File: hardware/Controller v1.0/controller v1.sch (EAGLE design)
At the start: 36 parts, among them CON1 1X08-CONN3.5MM, CON2 1X08-CONN3.5MM, CON3 1X08-CONN3.5MM, CON4 1X08-CONN3.5MM, IC1 MC33880PEG, IC2 L293DD, IC3 MC33880PEG

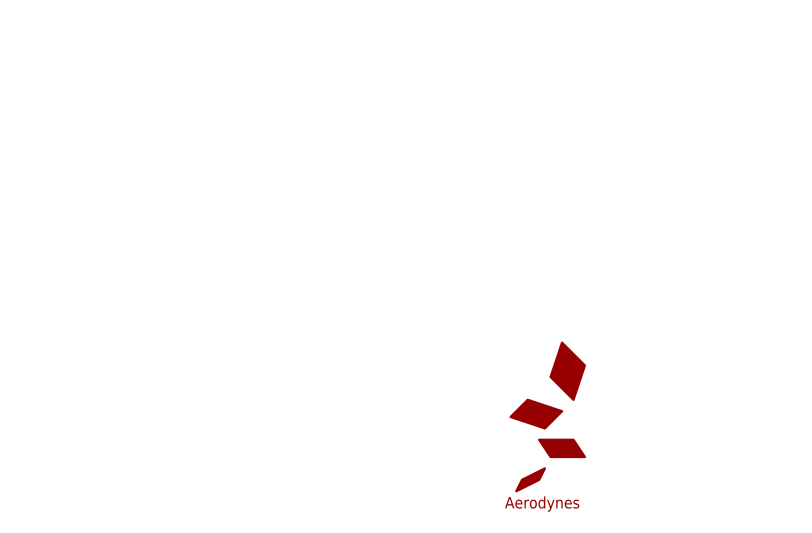
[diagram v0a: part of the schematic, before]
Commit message: Added license/author into on schematics
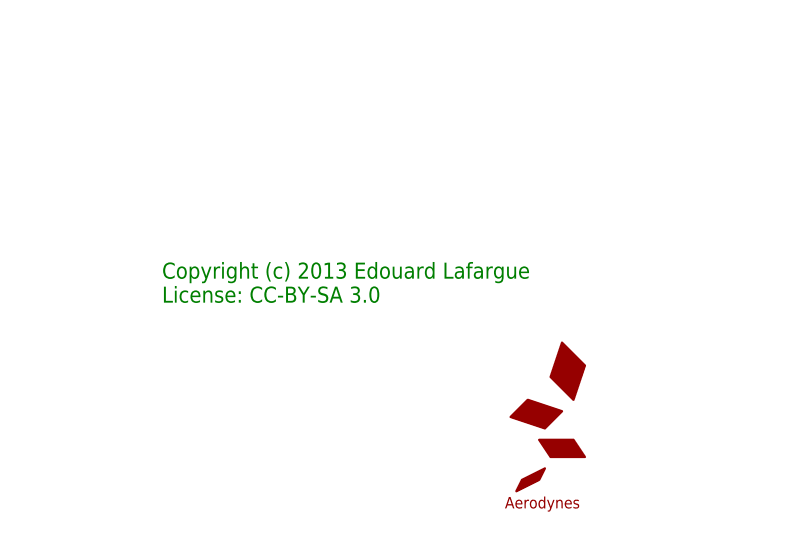
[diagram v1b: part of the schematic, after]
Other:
- note added: "Copyright (c) 2013 Edouard Lafargue License: CC-BY-SA 3.0"
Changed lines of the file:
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@@
 <text x="129.54" y="-40.64" size="1.778" layer="91">R6 at 10k leads to CURR_MEASURE
 at 5V for 1A input current.</text>
+<text x="256.54" y="-22.86" size="1.778" layer="91">Copyright (c) 2013 Edouard Lafargue
+License: CC-BY-SA 3.0</text>
 </plain>
 <instances>

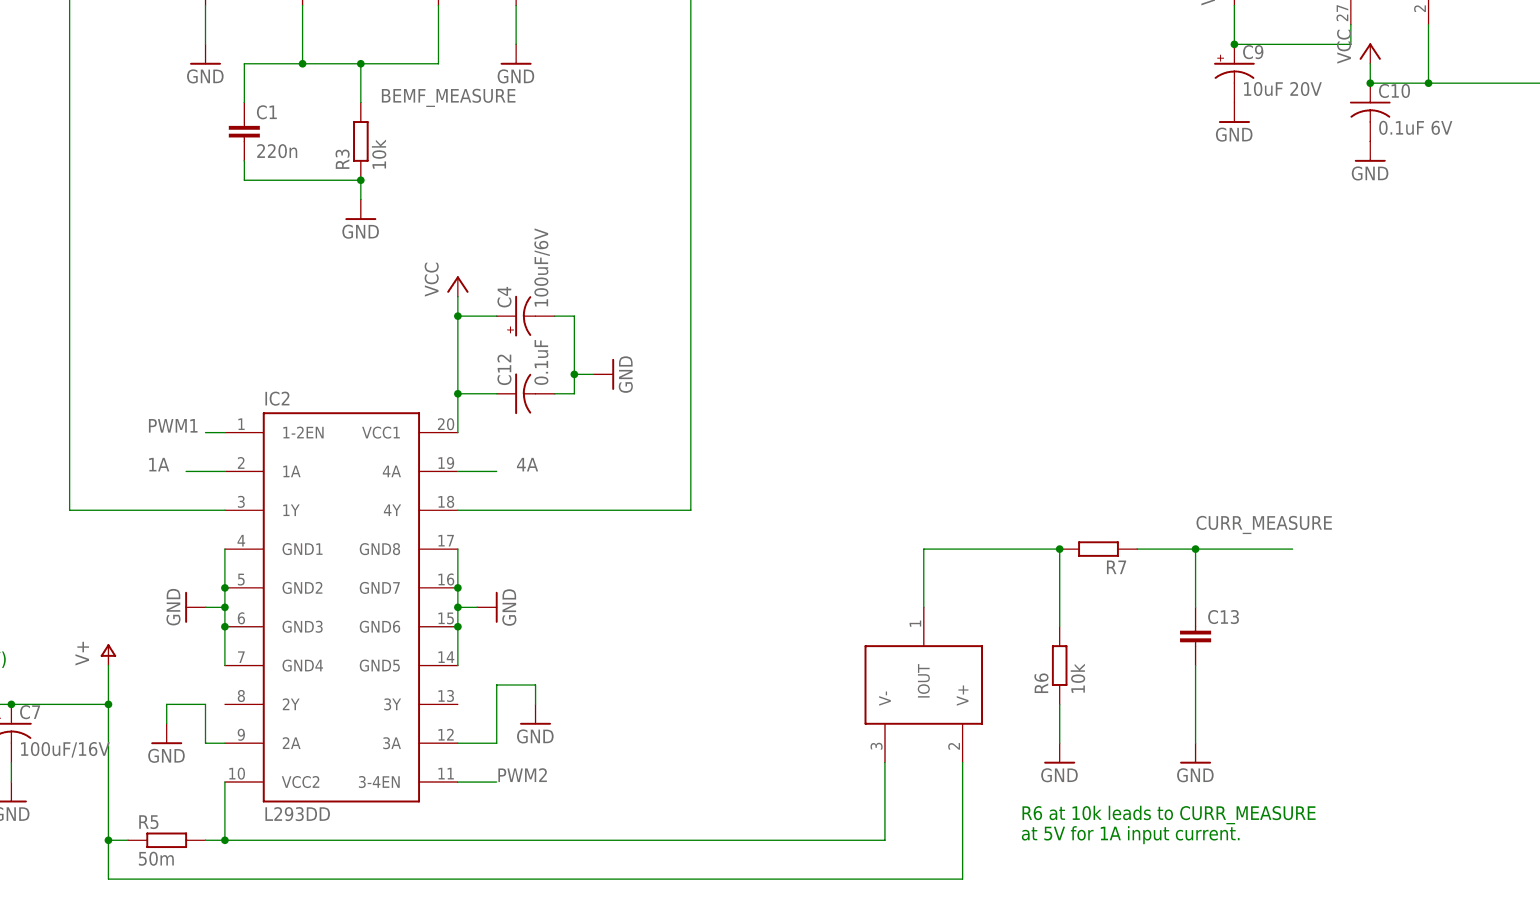
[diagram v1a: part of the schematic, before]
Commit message: Updates to match exactly first working prototype
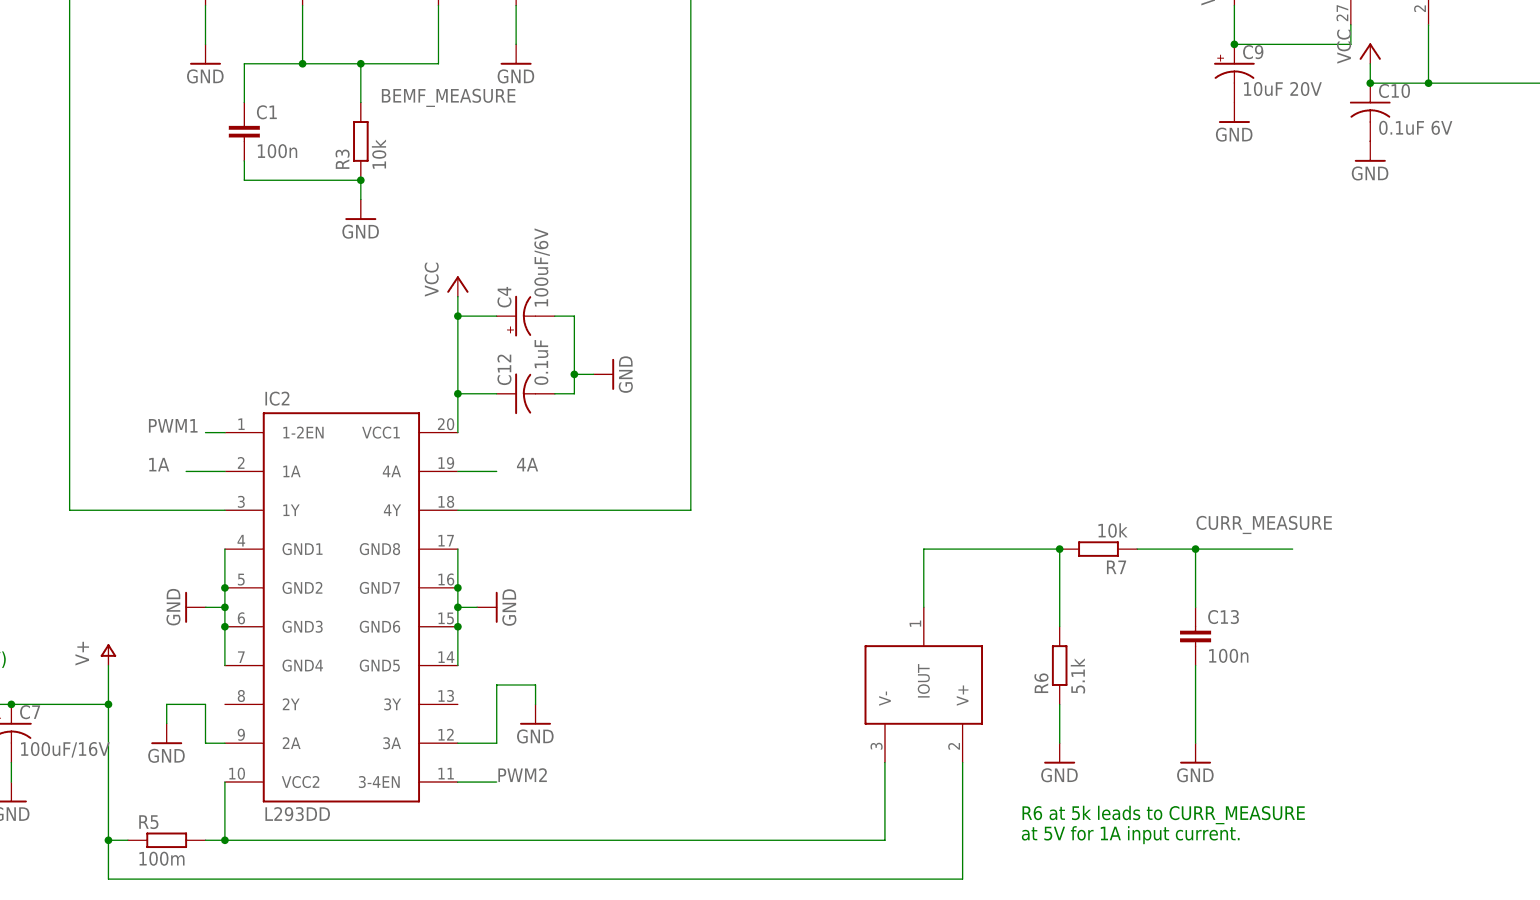
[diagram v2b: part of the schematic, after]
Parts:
- C1: value 220n -> 100n
- C13: value (none) -> 100n
- R5: value 50m -> 100m
- R6: value 10k -> 5.1k
- R7: value (none) -> 10k
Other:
- note added: "R6 at 5k leads to CURR_MEASURE at 5V for 1A input current."
- note removed: "R6 at 10k leads to CURR_MEASURE at 5V for 1A input current."
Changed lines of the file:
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@@
 <part name="SL2" library="adafruit" deviceset="1X2" device="-3.5MM"/>
 <part name="GND5" library="supply1" deviceset="GND" device=""/>
-<part name="C1" library="resistor" deviceset="C-EU" device="C0805" value="220n"/>
+<part name="C1" library="resistor" deviceset="C-EU" device="C0805" value="100n"/>
 <part name="C2" library="rcl-ez" deviceset="C-US" device="025-025X050" value="0.1uF"/>
 <part name="GND6" library="supply1" deviceset="GND" device=""/>
@@
 <part name="GND19" library="supply1" deviceset="GND" device=""/>
 <part name="GND20" library="supply1" deviceset="GND" device=""/>
-<part name="R5" library="resistor" deviceset="R-EU_" device="M1206" value="50m"/>
-<part name="R6" library="resistor" deviceset="R-EU_" device="R0603" value="10k"/>
-<part name="R7" library="resistor" deviceset="R-EU_" device="R0603"/>
+<part name="R5" library="resistor" deviceset="R-EU_" device="M1206" value="100m"/>
+<part name="R6" library="resistor" deviceset="R-EU_" device="R0603" value="5.1k"/>
+<part name="R7" library="resistor" deviceset="R-EU_" device="R0603" value="10k"/>
 <part name="GND21" library="supply1" deviceset="GND" device=""/>
 <part name="GND22" library="supply1" deviceset="GND" device=""/>
-<part name="C13" library="resistor" deviceset="C-EU" device="C0805K"/>
+<part name="C13" library="resistor" deviceset="C-EU" device="C0805K" value="100n"/>
 <part name="U$3" library="aerodynes" deviceset="ZXCT1009" device="-F"/>
 <part name="JP1" library="jumper" deviceset="JP1E" device=""/>
@@
 <text x="228.6" y="132.08" size="1.778" layer="91">Bank 4</text>
 <text x="144.78" y="203.2" size="1.778" layer="91">"wire to board Eurostyle terminal blocks"</text>
-<text x="129.54" y="-40.64" size="1.778" layer="91">R6 at 10k leads to CURR_MEASURE
+<text x="129.54" y="-40.64" size="1.778" layer="91">R6 at 5k leads to CURR_MEASURE
 at 5V for 1A input current.</text>
 <text x="256.54" y="-22.86" size="1.778" layer="91">Copyright (c) 2013 Edouard Lafargue

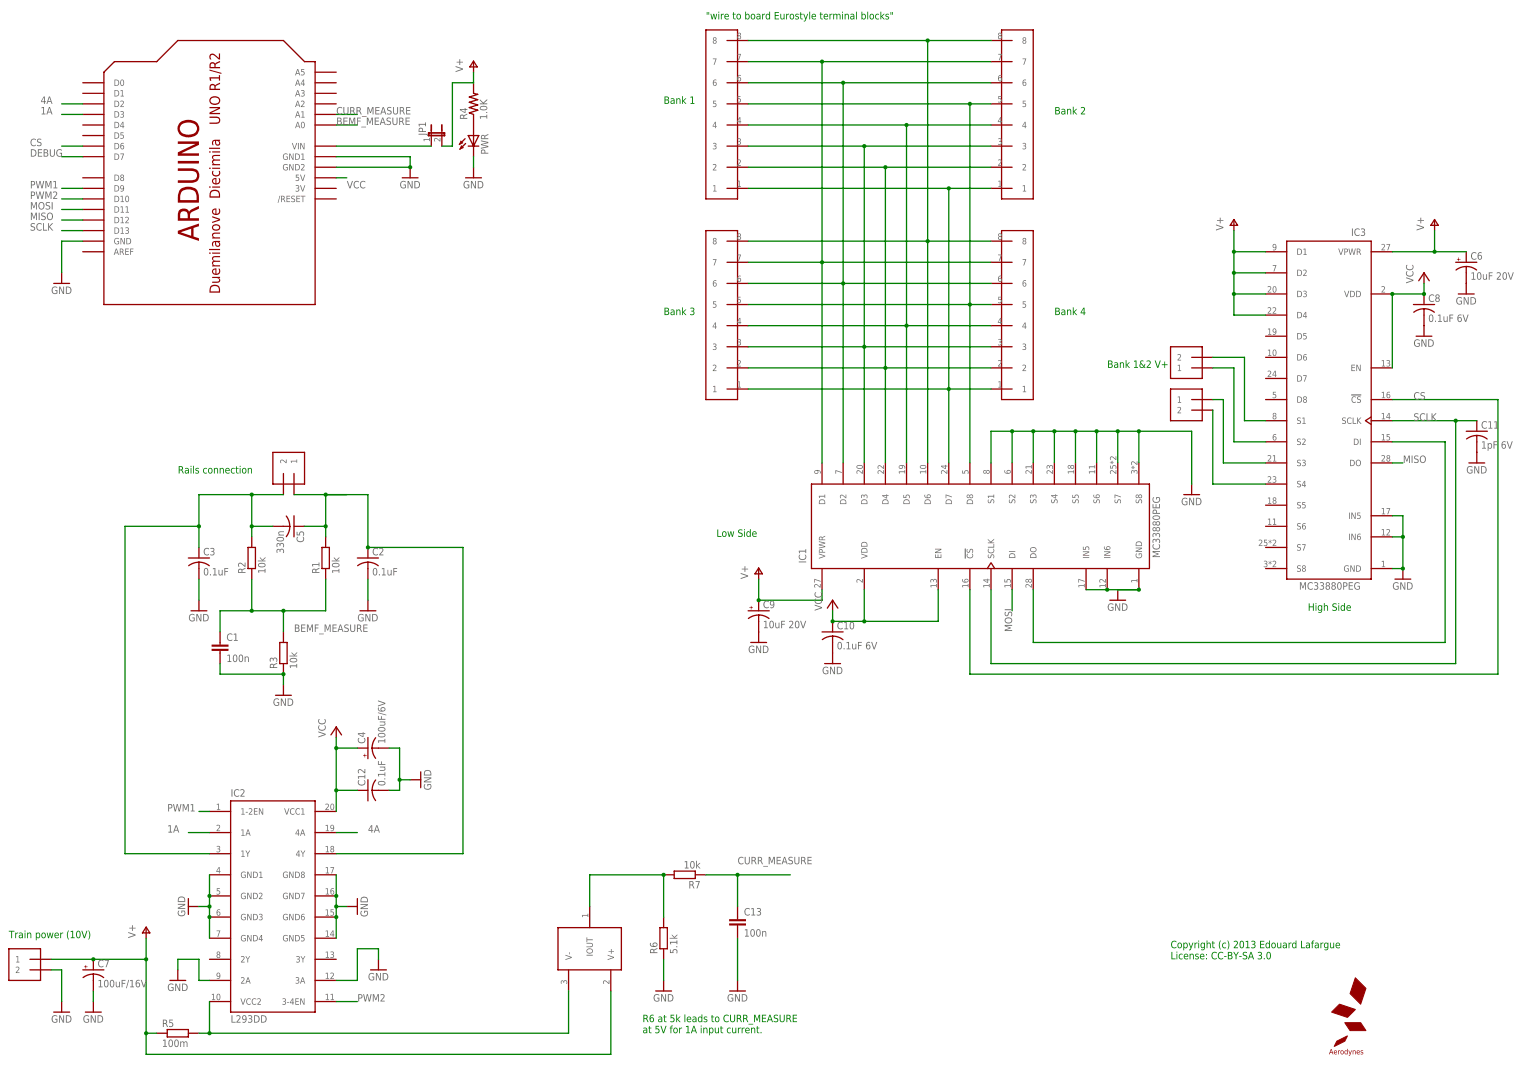
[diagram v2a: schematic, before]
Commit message: Another slight update for component values
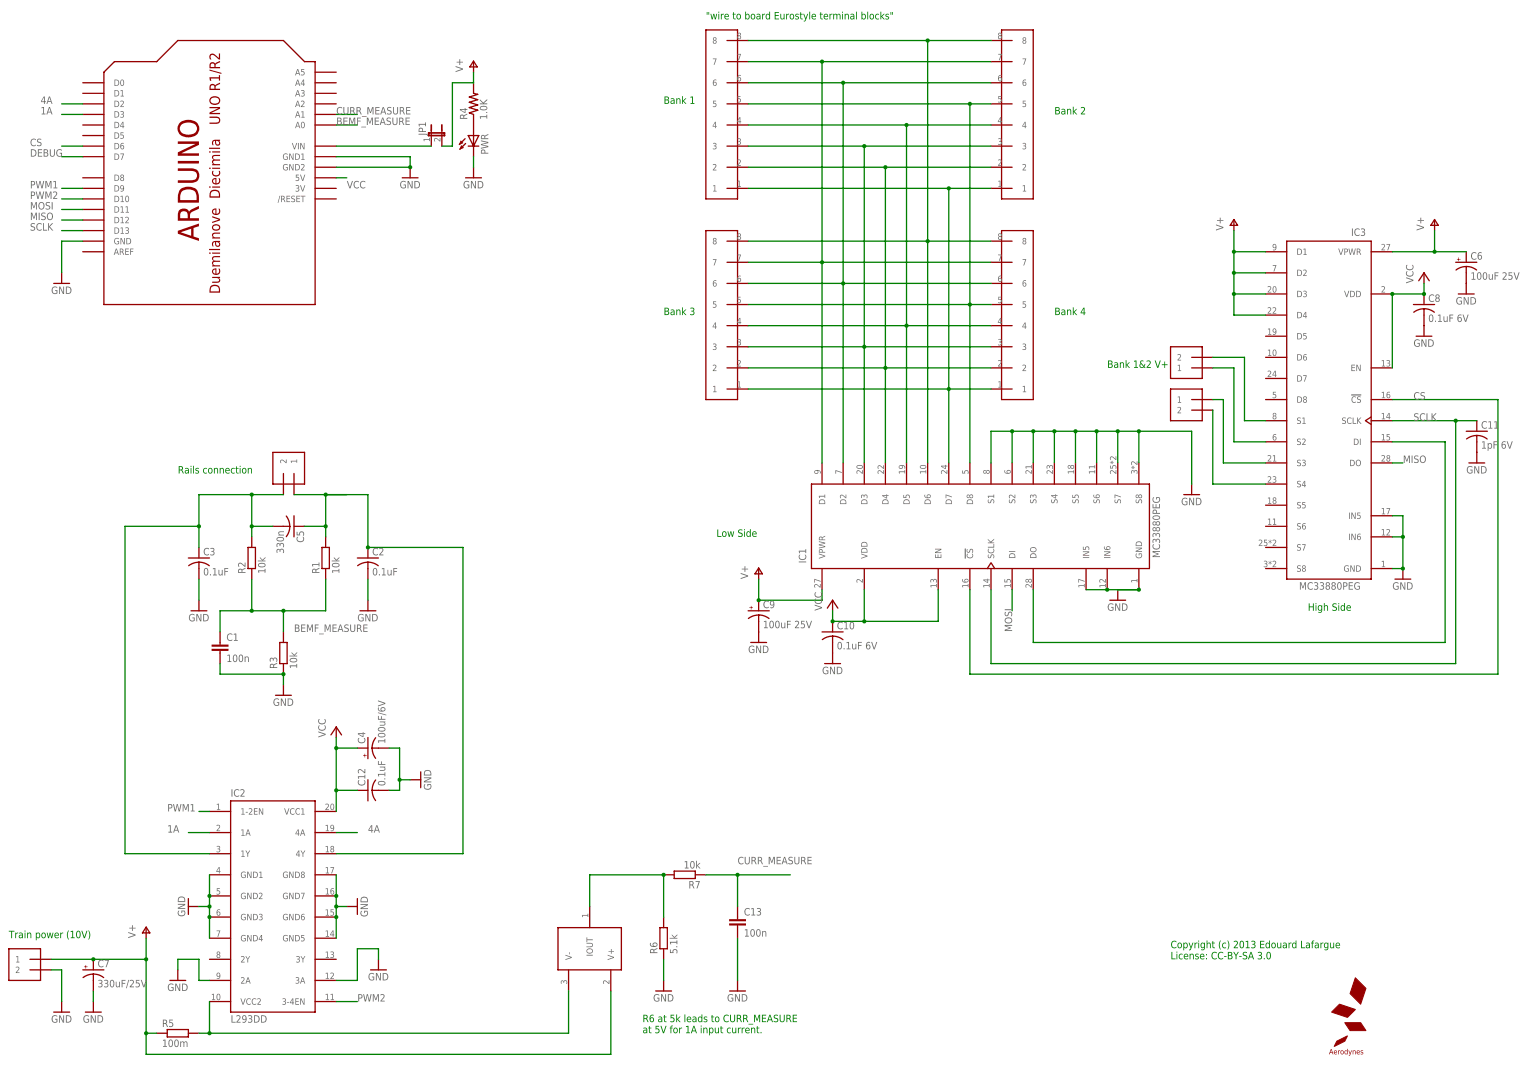
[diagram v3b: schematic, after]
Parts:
- C6, C9: value 10uF 20V -> 100uF 25V
- C7: value 100uF/16V -> 330uF/25V
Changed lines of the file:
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@@
 <part name="GND18" library="supply1" deviceset="GND" device=""/>
 <part name="P+9" library="supply1" deviceset="V+" device=""/>
-<part name="C7" library="rcl-ez" deviceset="CPOL-US" device="E2.5-6" value="100uF/16V"/>
+<part name="C7" library="rcl-ez" deviceset="CPOL-US" device="E2.5-6" value="330uF/25V"/>
 <part name="R1" library="resistor" deviceset="R-EU_" device="R0805" value="10k"/>
 <part name="R2" library="resistor" deviceset="R-EU_" device="R0805" value="10k"/>
@@
 <part name="+5V2" library="supply1" deviceset="VCC" device=""/>
 <part name="GND9" library="supply1" deviceset="GND" device=""/>
-<part name="C6" library="rcl" deviceset="CPOL-US" device="E2,5-6E" value="10uF 20V"/>
+<part name="C6" library="rcl" deviceset="CPOL-US" device="E2,5-6E" value="100uF 25V"/>
 <part name="C8" library="rcl-ez" deviceset="C-US" device="025-025X050" value="0.1uF 6V"/>
 <part name="GND10" library="supply1" deviceset="GND" device=""/>
@@
 <part name="GND8" library="supply1" deviceset="GND" device=""/>
 <part name="P+3" library="supply1" deviceset="V+" device=""/>
-<part name="C9" library="rcl" deviceset="CPOL-US" device="E2,5-6E" value="10uF 20V"/>
+<part name="C9" library="rcl" deviceset="CPOL-US" device="E2,5-6E" value="100uF 25V"/>
 <part name="GND12" library="supply1" deviceset="GND" device=""/>
 <part name="+5V3" library="supply1" deviceset="VCC" device=""/>

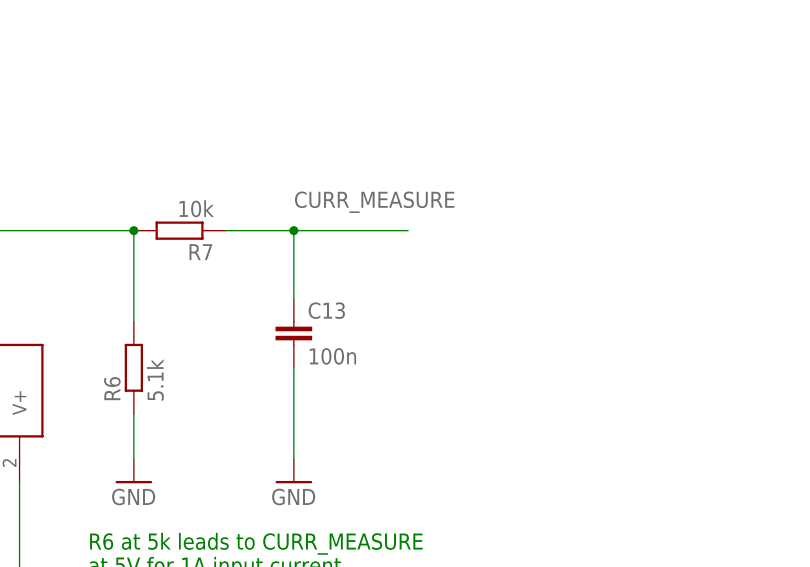
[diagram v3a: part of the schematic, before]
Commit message: Add support for current sensor.
All values output by the controller are now in real units (mV for BEMF
and mA for current). Web app graphs current value. Better graphs (no
gaps when sending turnout commands).
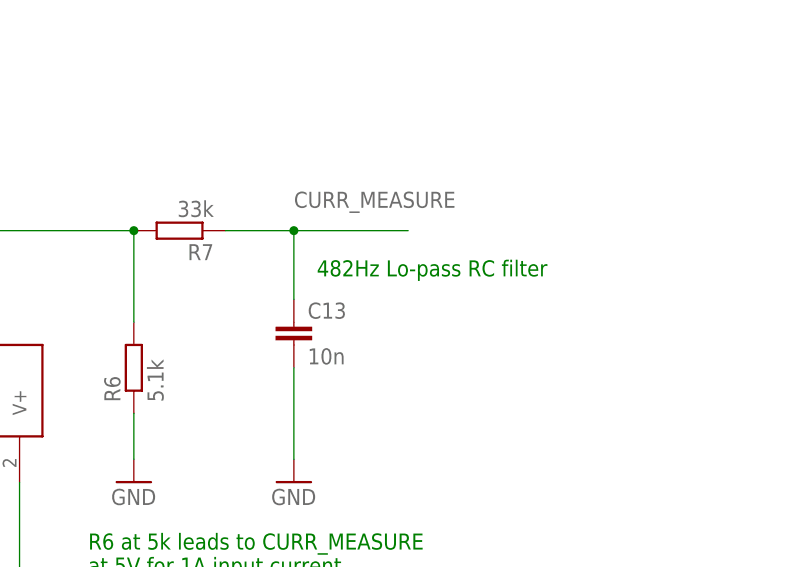
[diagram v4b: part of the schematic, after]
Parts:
- C13: value 100n -> 10n
- R7: value 10k -> 33k
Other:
- note added: "482Hz Lo-pass RC filter"
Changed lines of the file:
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@@
 <part name="R5" library="resistor" deviceset="R-EU_" device="M1206" value="100m"/>
 <part name="R6" library="resistor" deviceset="R-EU_" device="R0603" value="5.1k"/>
-<part name="R7" library="resistor" deviceset="R-EU_" device="R0603" value="10k"/>
+<part name="R7" library="resistor" deviceset="R-EU_" device="R0603" value="33k"/>
 <part name="GND21" library="supply1" deviceset="GND" device=""/>
 <part name="GND22" library="supply1" deviceset="GND" device=""/>
-<part name="C13" library="resistor" deviceset="C-EU" device="C0805K" value="100n"/>
+<part name="C13" library="resistor" deviceset="C-EU" device="C0805K" value="10n"/>
 <part name="U$3" library="aerodynes" deviceset="ZXCT1009" device="-F"/>
 <part name="JP1" library="jumper" deviceset="JP1E" device=""/>
@@
 <text x="256.54" y="-22.86" size="1.778" layer="91">Copyright (c) 2013 Edouard Lafargue
 License: CC-BY-SA 3.0</text>
+<text x="154.94" y="-7.62" size="1.778" layer="91">482Hz Lo-pass RC filter</text>
 </plain>
 <instances>
